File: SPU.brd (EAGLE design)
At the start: 160 x 130 mm, 414 parts, among them Q1 BSS123, Q2 12MHz, Q3 BSS123, Q4 BSS123, Q5 BSS123, Q6 BSS123

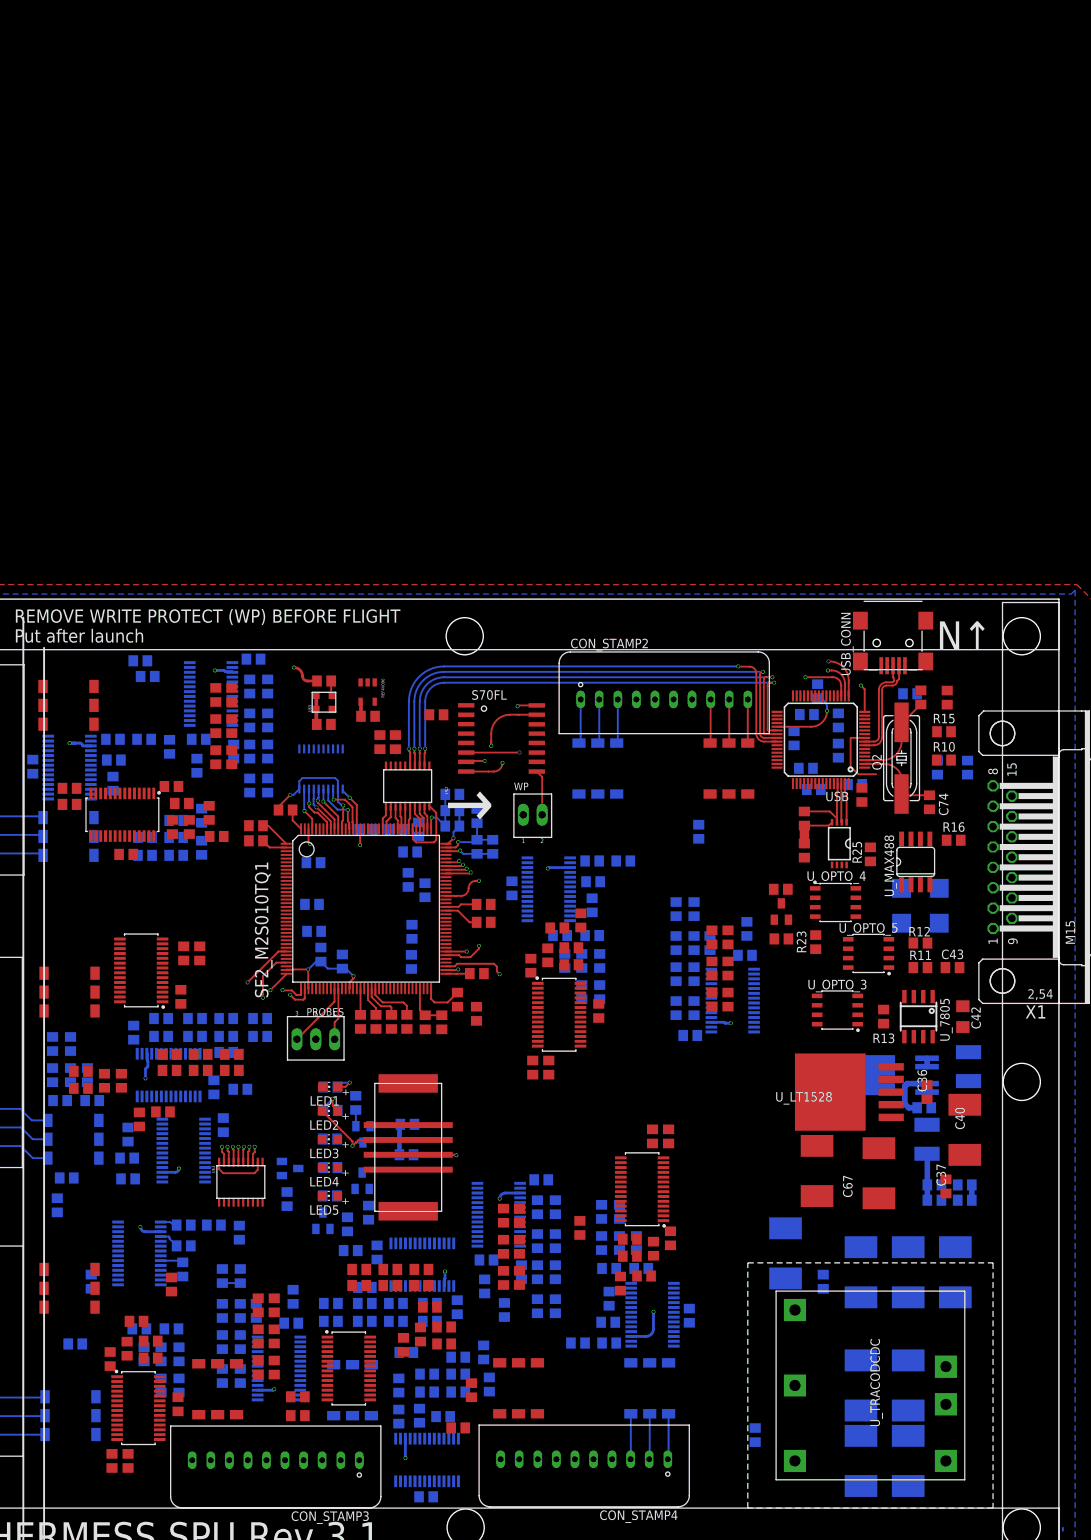
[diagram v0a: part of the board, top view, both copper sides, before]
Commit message: Schematic: changed names from STAMP2 - STMAP6 to STAMPN_ADC_SG/TEMP Bord: Adding names for more readabilty.
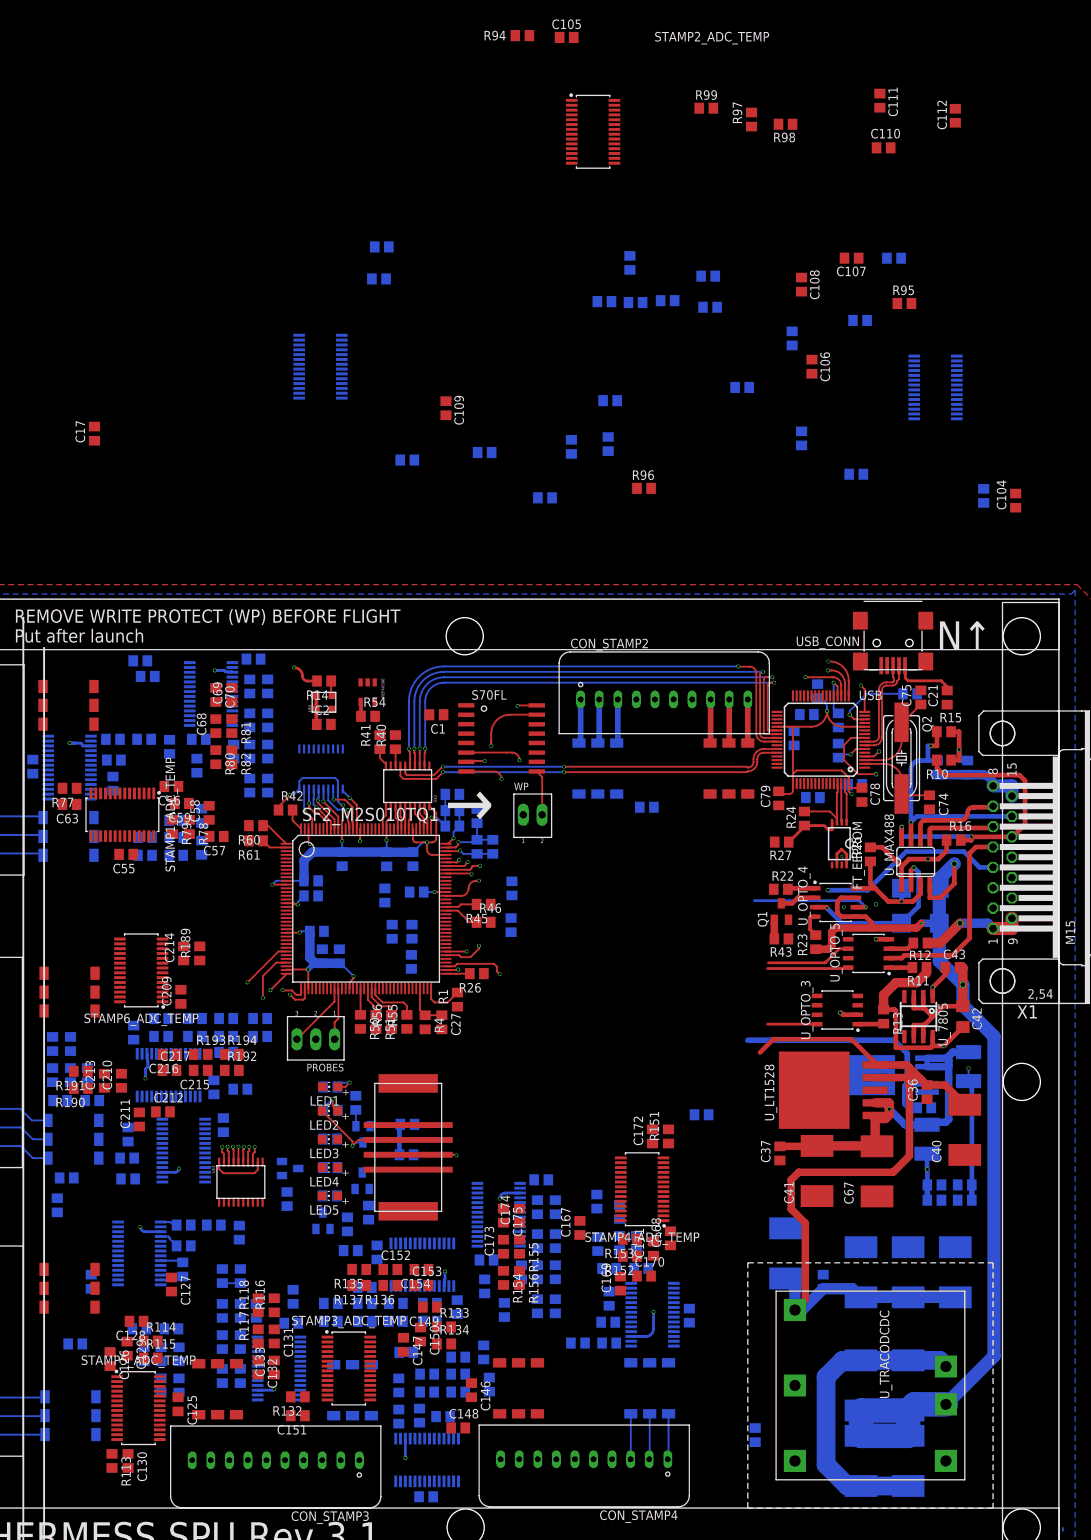
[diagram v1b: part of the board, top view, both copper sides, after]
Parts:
- removed STAMP1_ADC_SG5, STAMP1_ADC_SG6, STAMP1_ADC_TEMP2: ADS1148QPWRQ1, ads11xx:TSSOP28
- added STAMP2_ADC_SG1, STAMP2_ADC_SG2, STAMP2_ADC_TEMP: ADS1148QPWRQ1, ads11xx:TSSOP28
- moved R94 138.9 mm to (87.8, 205.9), turned to 180 degrees
- moved C105 125.1 mm to (93.7, 205.6), turned to 180 degrees
- moved C111 123.1 mm to (135.9, 197.1)
- moved C112 122.9 mm to (146.1, 195.1)
- moved R98 114.1 mm to (123.2, 193.9), turned to 180 degrees
- moved C110 112.5 mm to (136.4, 190.8), turned to 0 degrees
- moved R99 111.6 mm to (112.5, 196.1), turned to 0 degrees
- moved R97 110.2 mm to (118.6, 194.6)
- moved C101 101.7 mm to (137.8, 175.9)
- moved C107 98.5 mm to (132.1, 175.9)
- moved R95 97.6 mm to (139.2, 169.8)
- moved C108 96.5 mm to (125.3, 172.3)
- moved R90 95.0 mm to (133.2, 167.5), turned to 180 degrees
- moved C17 93.5 mm to (30.1, 152.3)
- moved R85 91.8 mm to (102.2, 175.3)
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- renumbered STAMP1_ADC_SG10 to STAMP3_ADC_SG2, STAMP1_ADC_SG11 to STAMP4_ADC_SG1, STAMP1_ADC_SG12 to STAMP4_ADC_SG2, STAMP1_ADC_SG15 to STAMP6_ADC_SG1, STAMP1_ADC_SG16 to STAMP6_ADC_SG2, STAMP1_ADC_SG7 to STAMP5_ADC_SG1, STAMP1_ADC_SG8 to STAMP5_ADC_SG2, STAMP1_ADC_SG9 to STAMP3_ADC_SG1, STAMP1_ADC_TEMP3 to STAMP5_ADC_TEMP, STAMP1_ADC_TEMP4 to STAMP3_ADC_TEMP, STAMP1_ADC_TEMP5 to STAMP4_ADC_TEMP, STAMP1_ADC_TEMP7 to STAMP6_ADC_TEMP
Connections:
- removed net STAMP2_TEMP_AIN1: CON_STAMP2.P$4, R95.2, STAMP1_ADC_TEMP2.11
- new net SMASHALL: CON_STAMP2.P$4, R95.2, STAMP2_ADC_TEMP.11
- net 3V3: now also STAMP2_ADC_SG1.1, STAMP2_ADC_SG1.22, STAMP2_ADC_SG2.1, STAMP2_ADC_SG2.22, STAMP2_ADC_TEMP.1, STAMP2_ADC_TEMP.22; no longer STAMP1_ADC_SG5.1, STAMP1_ADC_SG5.22, STAMP1_ADC_SG6.1, STAMP1_ADC_SG6.22, STAMP1_ADC_TEMP2.1, STAMP1_ADC_TEMP2.22
- net ADC_START: now also STAMP2_ADC_SG1.23, STAMP2_ADC_SG2.23, STAMP2_ADC_TEMP.23; no longer STAMP1_ADC_SG5.23, STAMP1_ADC_SG6.23, STAMP1_ADC_TEMP2.23
- net GND: now also STAMP2_ADC_SG1.10, STAMP2_ADC_SG1.2, STAMP2_ADC_SG1.21, STAMP2_ADC_SG2.10, STAMP2_ADC_SG2.2, STAMP2_ADC_SG2.21, STAMP2_ADC_TEMP.10, STAMP2_ADC_TEMP.2, STAMP2_ADC_TEMP.21, STAMP2_ADC_TEMP.3; no longer STAMP1_ADC_SG5.10, STAMP1_ADC_SG5.2, STAMP1_ADC_SG5.21, STAMP1_ADC_SG6.10, STAMP1_ADC_SG6.2, STAMP1_ADC_SG6.21, STAMP1_ADC_TEMP2.10, STAMP1_ADC_TEMP2.2, STAMP1_ADC_TEMP2.21, STAMP1_ADC_TEMP2.3
- net N$100: now also STAMP2_ADC_SG2.26; no longer STAMP1_ADC_SG6.26
- net N$101: now also STAMP2_ADC_SG2.11; no longer STAMP1_ADC_SG6.11
- net N$102: now also STAMP2_ADC_SG2.12; no longer STAMP1_ADC_SG6.12
- net N$105: now also STAMP2_ADC_TEMP.26; no longer STAMP1_ADC_TEMP2.26
- net N$106: now also STAMP2_ADC_TEMP.4; no longer STAMP1_ADC_TEMP2.4
- net N$107: now also STAMP2_ADC_TEMP.12; no longer STAMP1_ADC_TEMP2.12
- net N$108: now also STAMP2_ADC_TEMP.17; no longer STAMP1_ADC_TEMP2.17
- net N$109: now also STAMP2_ADC_TEMP.9; no longer STAMP1_ADC_TEMP2.9
- net N$110: now also STAMP2_ADC_TEMP.6; no longer STAMP1_ADC_TEMP2.6
- net N$111: now also STAMP2_ADC_TEMP.5; no longer STAMP1_ADC_TEMP2.5
- net N$78: now also STAMP2_ADC_SG1.4; no longer STAMP1_ADC_SG5.4
- net N$85: now also STAMP2_ADC_SG1.9; no longer STAMP1_ADC_SG5.9
- net N$93: now also STAMP2_ADC_SG1.26; no longer STAMP1_ADC_SG5.26
- net N$94: now also STAMP2_ADC_SG1.11; no longer STAMP1_ADC_SG5.11
- net N$95: now also STAMP2_ADC_SG1.12; no longer STAMP1_ADC_SG5.12
- net N$98: now also STAMP2_ADC_SG2.4; no longer STAMP1_ADC_SG6.4
- net N$99: now also STAMP2_ADC_SG2.9; no longer STAMP1_ADC_SG6.9
- net SG_CLK: now also STAMP2_ADC_SG1.3, STAMP2_ADC_SG2.3; no longer STAMP1_ADC_SG5.3, STAMP1_ADC_SG6.3
- net STAMP2_CS_SG1: now also STAMP2_ADC_SG1.24; no longer STAMP1_ADC_SG5.24
- net STAMP2_CS_SG2: now also STAMP2_ADC_SG2.24; no longer STAMP1_ADC_SG6.24
- net STAMP2_CS_TEMP: now also STAMP2_ADC_TEMP.24; no longer STAMP1_ADC_TEMP2.24
- net STAMP2_DRDY_SG1: now also STAMP2_ADC_SG1.25; no longer STAMP1_ADC_SG5.25
- net STAMP2_DRDY_SG2: now also STAMP2_ADC_SG2.25; no longer STAMP1_ADC_SG6.25
- net STAMP2_DRDY_TEMP: now also STAMP2_ADC_TEMP.25; no longer STAMP1_ADC_TEMP2.25
- net STAMP2_MOSI: now also STAMP2_ADC_SG1.27, STAMP2_ADC_SG2.27, STAMP2_ADC_TEMP.27; no longer STAMP1_ADC_SG5.27, STAMP1_ADC_SG6.27, STAMP1_ADC_TEMP2.27
- net STAMP2_SCLK: now also STAMP2_ADC_SG1.28, STAMP2_ADC_SG2.28, STAMP2_ADC_TEMP.28; no longer STAMP1_ADC_SG5.28, STAMP1_ADC_SG6.28, STAMP1_ADC_TEMP2.28
- net STAMP2_TEMP_AIN2: now also STAMP2_ADC_TEMP.18; no longer STAMP1_ADC_TEMP2.18
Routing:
- net 28VGND: track 0.00 -> 190.5 mm, vias 0 -> 3
- net 28V: track 0.00 -> 145.0 mm, vias 0 -> 2
- net 5V: track 4.14 -> 120.7 mm
- net 1V2: track 60.7 -> 135.6 mm, vias 4 -> 10
- net N$16: track 2.06 -> 67.8 mm, vias 0 -> 2
- net 3V3: track 7.40 -> 70.5 mm, vias 0 -> 3
- net N$180: track 15.8 -> 74.8 mm, vias 0 -> 2
- net DAPI_DTR: track 0.00 -> 53.9 mm, vias 0 -> 2
- net DAPI_DSR: track 0.00 -> 52.9 mm, vias 0 -> 2
- net SG_CLK: track 396.5 -> 344.8 mm, vias 13 -> 11
- net RXSM_SOE: track 0.00 -> 44.9 mm, vias 0 -> 2
- net EXP_IN_P: track 0.00 -> 41.7 mm, vias 0 -> 2
- net 5V-NONISO: track 0.00 -> 37.7 mm, vias 0 -> 2
- net EXP_IN_N: track 0.00 -> 32.4 mm, vias 0 -> 2
- net N$179: track 9.85 -> 40.4 mm, vias 1 -> 2
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
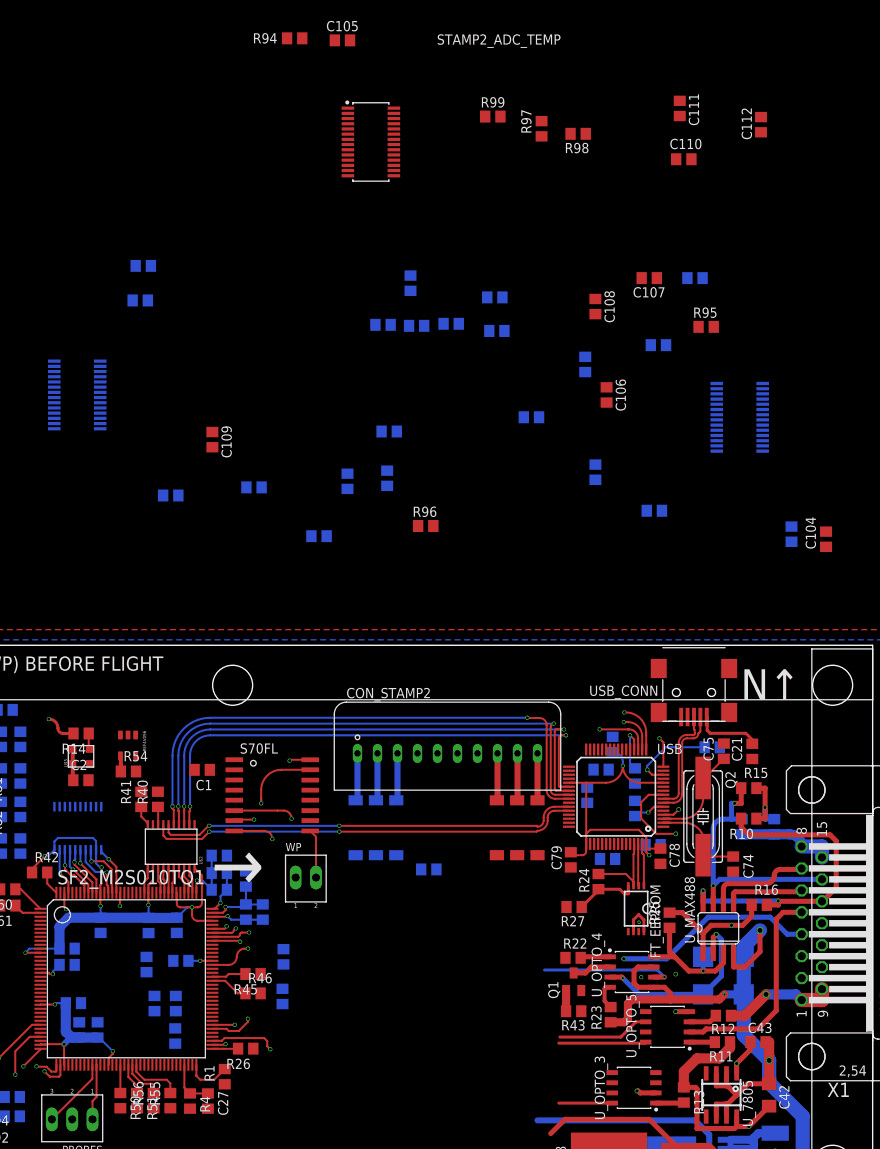
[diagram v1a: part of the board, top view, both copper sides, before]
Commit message: End of day commit Schematic: Removed renaming error Bord: Placed and routed Stamp 2
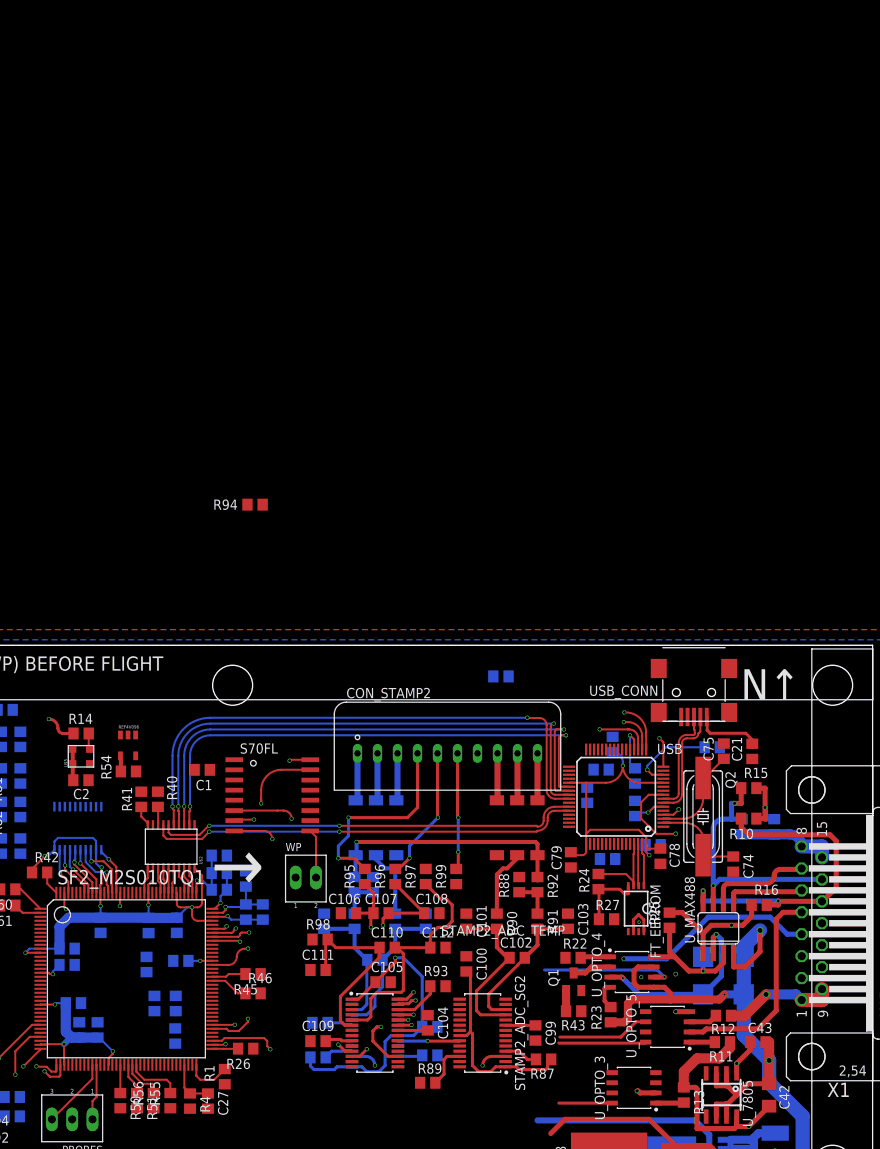
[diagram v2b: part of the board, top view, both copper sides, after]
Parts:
- moved C105 117.8 mm to (98.8, 87.9), turned to 0 degrees
- moved C111 116.8 mm to (90.7, 89.4), turned to 180 degrees
- moved STAMP2_ADC_TEMP 111.4 mm to (97.8, 81.5)
- moved R87 111.1 mm to (118.9, 78.2), flipped to the top
- moved C112 110.5 mm to (105.7, 92.2), turned to 180 degrees
- moved R98 105.8 mm to (90.9, 93.2)
- moved C110 105.3 mm to (99.3, 92.2), turned to 180 degrees
- moved R99 95.1 mm to (108.0, 101.1), turned to 90 degrees
- moved R97 94.6 mm to (104.1, 101.1)
- moved STAMP2_ADC_SG2 94.5 mm to (111.3, 81.5), flipped to the top, turned to 180 degrees
- moved R93 93.5 mm to (105.7, 87.4), flipped to the top, turned to 180 degrees
- moved STAMP2_ADC_SG1 89.5 mm to (97.8, 81.5)
- moved C107 86.2 mm to (98.6, 96.5), turned to 0 degrees
- moved C101 85.3 mm to (109.2, 95.5), flipped to the top, turned to 270 degrees
- moved C99 83.8 mm to (117.9, 81.5), flipped to the top
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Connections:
- net N$110 renamed S2AT2
- net N$111 renamed S2AT1
- net SMASHALL renamed STAMP2_TEMP_AIN1
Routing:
- net 3V3: track 70.5 -> 137.5 mm, vias 3 -> 4
- net STAMP2_TEMP_AIN1: track 0.00 -> 50.7 mm, vias 0 -> 3
- net 4V096: track 1.98 -> 33.7 mm, vias 0 -> 1
- net N$108: track 0.00 -> 31.5 mm, vias 0 -> 2
- net S2AT1: track 0.00 -> 30.8 mm
- net SG_CLK: track 344.8 -> 371.1 mm, vias 11 -> 13
- net N$107: track 0.00 -> 25.8 mm, vias 0 -> 2
- net S2AT2: track 0.00 -> 23.7 mm
- net N$101: track 0.00 -> 20.4 mm
- net N$102: track 0.00 -> 18.3 mm
- net N$94: track 0.00 -> 17.9 mm
- net STAMP2_TEMP_AIN2: track 0.00 -> 16.9 mm, vias 0 -> 2
- net N$95: track 0.00 -> 16.1 mm
- net STAMP2_TEMP_AIN3: track 0.00 -> 14.6 mm, vias 0 -> 2
- net ADC_START: track 0.00 -> 12.3 mm, vias 0 -> 2
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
